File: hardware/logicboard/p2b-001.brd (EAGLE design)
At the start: 91 x 90 mm, 55 parts, among them IC1 74LS06N, IC2 4066N, J1 MKR, J2 GPIO, J3 Vcc, J4 RLY, J5 SPI, J7 DIN5, J8 DIN5, J9 DIN5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

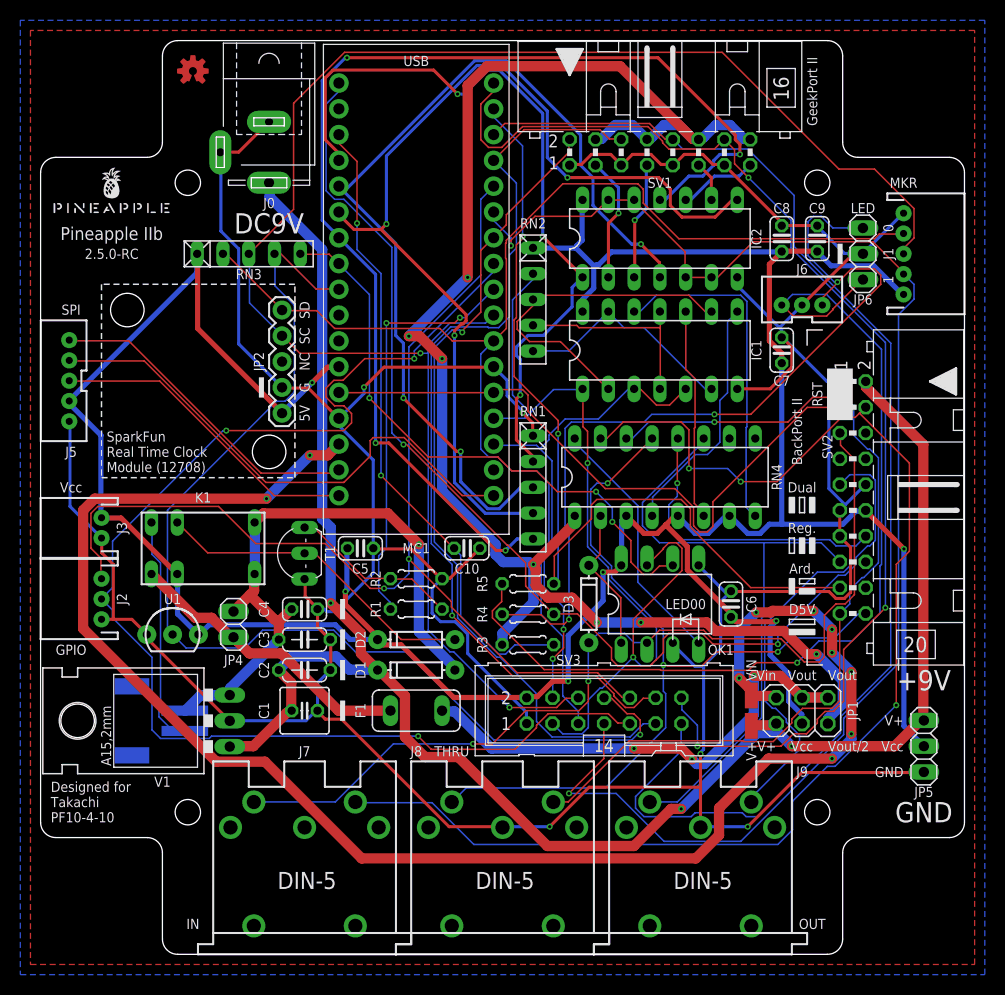
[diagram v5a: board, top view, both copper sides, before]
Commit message: Added holes for backport ii.
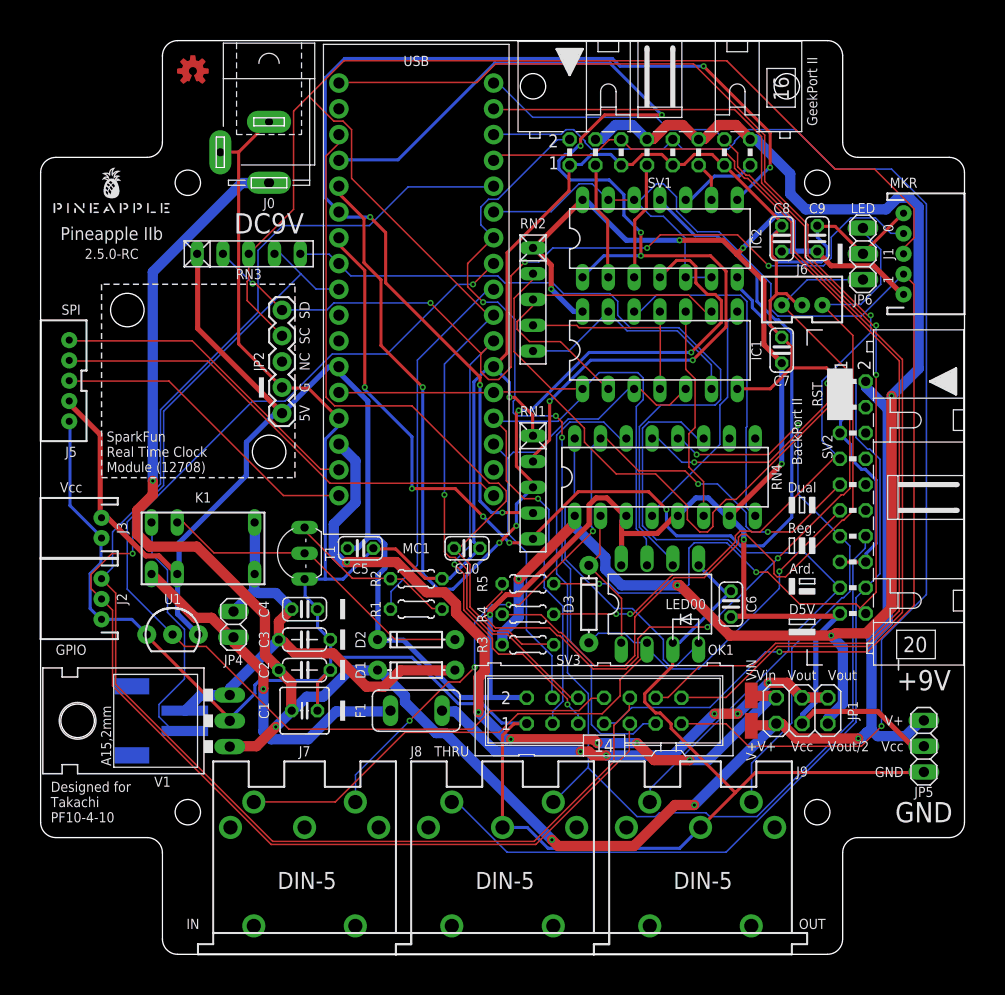
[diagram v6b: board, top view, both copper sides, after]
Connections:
- net GND: now also SV2.15, SV2.16, SV2.5; no longer SV2.10, SV2.11, SV2.13
- net LED0: now also SV2.7; no longer SV2.9
- net LED1: now also SV2.20; no longer SV2.17
- net MIRTN: now also SV2.11; no longer SV2.5
- net MISND: now also SV2.9; no longer SV2.4
- net MORTN: now also SV2.17; no longer SV2.15
- net MOSND: now also SV2.13; no longer SV2.14
- net MRXDTCT: now also SV2.4; no longer SV2.7
- net MTRTN: now also SV2.18; no longer SV2.20
- net MTSND: now also SV2.14; no longer SV2.19
- net MTX+: now also SV2.10; no longer SV2.16
- net MTX-: now also SV2.12; no longer SV2.18
- net VCC: now also SV2.19; no longer SV2.12
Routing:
- net VIN: track 162.8 -> 74.9 mm, vias 10 -> 6
- net MISND: track 128.2 -> 78.3 mm, vias 3 -> 6
- net ANLG0: track 74.7 -> 113.5 mm, vias 3 -> 6
- net GPIO1: track 111.8 -> 141.2 mm, vias 2 -> 0
- net LED1: track 89.0 -> 117.6 mm, vias 2 -> 4
- net MTRTN: track 80.9 -> 109.2 mm, vias 3 -> 2
- net GND: track 398.8 -> 415.4 mm, vias 5 -> 1
- net MNTR: track 58.2 -> 74.0 mm, vias 3 -> 0
- net LED1A: track 95.0 -> 80.4 mm, vias 1 -> 2
- net VCC/2: track 158.8 -> 144.7 mm, vias 7 -> 4
- net DTCT3: track 118.2 -> 104.3 mm, vias 3 -> 0
- net DTCT1: track 91.5 -> 104.2 mm, vias 1 -> 0
- net MIRTN: track 93.2 -> 81.1 mm, vias 2 -> 1
- net ANLG2: track 99.2 -> 110.8 mm, vias 3 -> 5
- net VOUTRAW: track 61.3 -> 50.0 mm, vias 1 -> 0
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- removed copper zone on layer 1, net GND
- removed copper zone on layer 16, net GND

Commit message: Added pogo pins to GeekPort II.
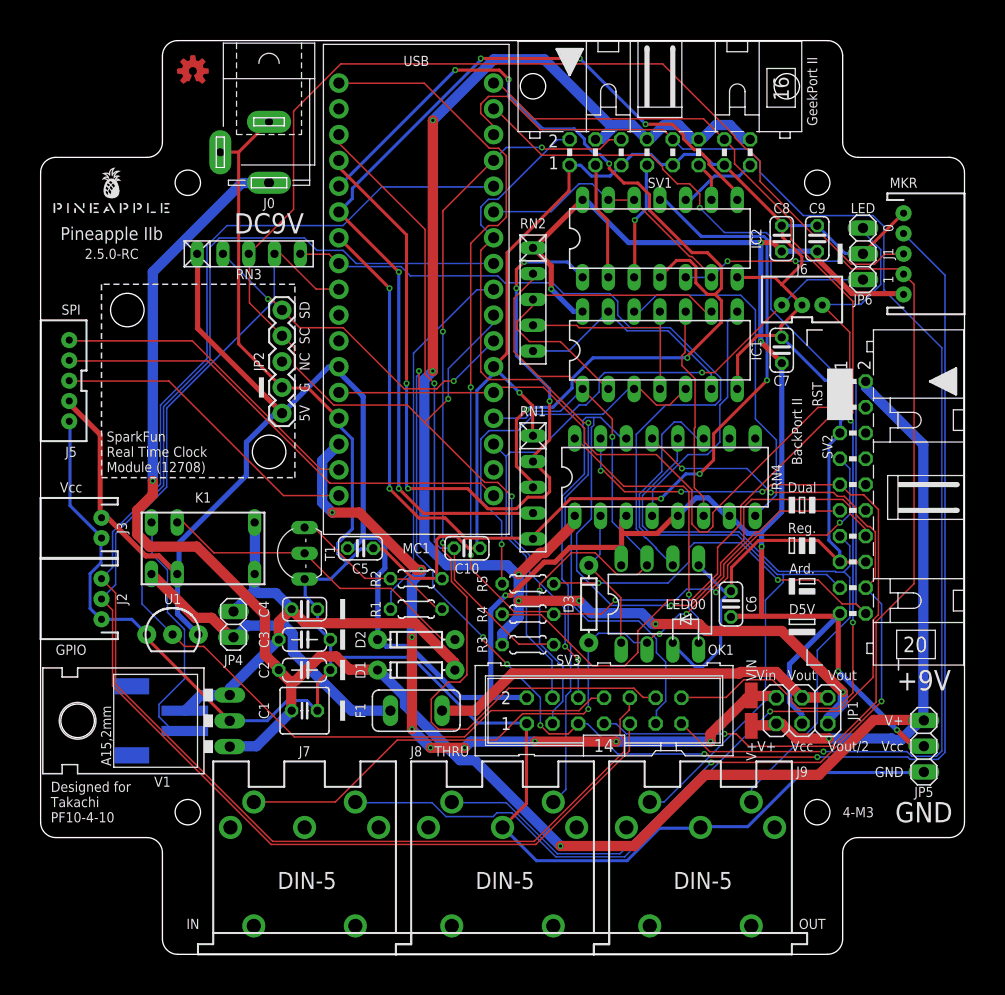
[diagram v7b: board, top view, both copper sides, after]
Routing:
- net SDA: track 137.6 -> 171.1 mm, vias 7 -> 8
- net MISND: track 78.3 -> 110.3 mm, vias 6 -> 4
- net ANLG0: track 113.5 -> 82.7 mm, vias 6 -> 5
- net LED1A: track 80.4 -> 60.1 mm
- net MTRTN: track 109.2 -> 94.6 mm, vias 2 -> 4
- net V+: track 192.2 -> 206.6 mm, vias 5 -> 3
- net ANLG2: track 110.8 -> 96.7 mm
- net GND: track 415.4 -> 402.3 mm
- net RX: track 87.9 -> 74.9 mm, vias 1 -> 2
- net SCL: track 176.3 -> 163.4 mm, vias 1 -> 4
- net ANLG3: track 111.9 -> 100.2 mm
- net GPIO0: track 130.0 -> 141.3 mm, vias 2 -> 0
- net D7GATE: track 133.8 -> 122.9 mm, vias 1 -> 4
- net AREF: track 72.4 -> 61.8 mm, vias 0 -> 1
- net LED0A: track 84.1 -> 75.0 mm
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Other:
- board text added: "4-M3"
